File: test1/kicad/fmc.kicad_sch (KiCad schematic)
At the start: 0 parts

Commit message: test1: fill in Power, Bias, Bobcat, Connectors, FMC sheets
Completes the test1 Bobcat carrier hierarchical schematic. All 7 sheets
(root + 6 children) parse cleanly with kicad-cli and render to SVG/PDF.

Contents per child:
  - power.kicad_sch       — TPS7A8401A LDO (3P3V → 0.8V via ANY-OUT
                            strap, OUT side fans to +VDDD/+VDDA1/+VDDA2
                            via 1×2 jumpers) + TPS22916 load switch
                            (VADJ → +VDDIO) with EN pulldowns + decoupling.
  - bobcat.kicad_sch      — Bobcat 40-QFN DUT with VDDD/VDDIO decoupling,
                            VDDA1/VDDA2 series 0Ω + decoupling, hier-label
                            exits on all four edges for SAMPLE_OUT*,
                            SPI, GPIO, CLK_OUT*, BIAS0/1, etc.
  - eeprom.kicad_sch      — 24AA08 I²C EEPROM (address 000, WP→GND,
                            0.1 µF decoupling, 2.2 kΩ I²C pull-ups).
  - bias.kicad_sch        — MCP4728 quad DAC + OPA2388 dual op-amp
                            (units 1 & 2) + PMZ1200UPEYL high-side PMOS
                            × 2 channels + 5.11 kΩ 0.1% sense resistors +
                            DNP 2N7002 isolation NMOS placeholders.
  - connectors.kicad_sch  — 4× SMA for CLK_OUT0–3, 3× SMA for
                            OSC_EN/WEIGHT_EN/SAMPLE_TRIG, 1×4 GPIO
                            header, 3× Keystone-5011 GND test clips.
  - fmc.kicad_sch         — VITA 57.1 LPC connector (4 units × 40 pins),
                            wired for 3P3V/VADJ/SCL/SDA/PRSNT/GA0/GA1/
                            PG_C2M/LDO_EN/LSW_EN; LA-bank pins NC'd for
                            later pinning; all other C/D/G/H pins to GND.

Generator improvements driven by this round:
  - Multi-unit symbol support (parse_pins now returns the per-pin unit
    number; place() takes a unit= parameter and emits matching (unit N)
    in the instance + path).
  - Escape backslash/quote in property values so refs/values with
    embedded " (e.g. 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
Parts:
- added J1: FMC LPC (C), Connector:FMC_LPC_ASP-134606-01, symbol Lib:ASP-134606-01
- added J2: FMC LPC (D), Connector:FMC_LPC_ASP-134606-01, symbol Lib:ASP-134606-01
- added J3: FMC LPC (G), Connector:FMC_LPC_ASP-134606-01, symbol Lib:ASP-134606-01
- added J4: FMC LPC (H), Connector:FMC_LPC_ASP-134606-01, symbol Lib:ASP-134606-01
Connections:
- new net +3V3: J1.C36, J1.C38, J1.C40, J2.D39
- new net GND: J1.C10, J1.C13, J1.C16, J1.C19, J1.C2, J1.C22, J1.C25, J1.C28, J1.C3, J1.C34, J1.C35, J1.C37, J1.C39, J1.C6, J1.C7, J2.D1, J2.D12, J2.D13, J2.D16, J2.D17, J2.D20, J2.D21, J2.D24, J2.D25, J2.D28, J2.D29, J2.D32, J2.D33, J2.D34, J2.D36, J2.D38, J2.D4, J2.D40, J2.D5, J2.D8, J2.D9, J3.G1, J3.G12, J3.G15, J3.G18, J3.G2, J3.G21, J3.G24, J3.G27, J3.G3, J3.G30, J3.G33, J3.G36, J3.G39, J3.G6, J3.G9, J4.H11, J4.H14, J4.H17, J4.H2, J4.H20, J4.H23, J4.H26, J4.H29, J4.H32, J4.H35, J4.H38, J4.H4, J4.H40, J4.H5, J4.H8
- new net LDO_PG: J1.C1
- new net SCL: J2.D30
- new net SDA: J2.D31
- new net VADJ: J3.G40, J4.H39
- no-connect marks 0 -> 85
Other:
- title: test1 — FMC Connector -> test1 — FMC LPC Connector (Power + I²C only)

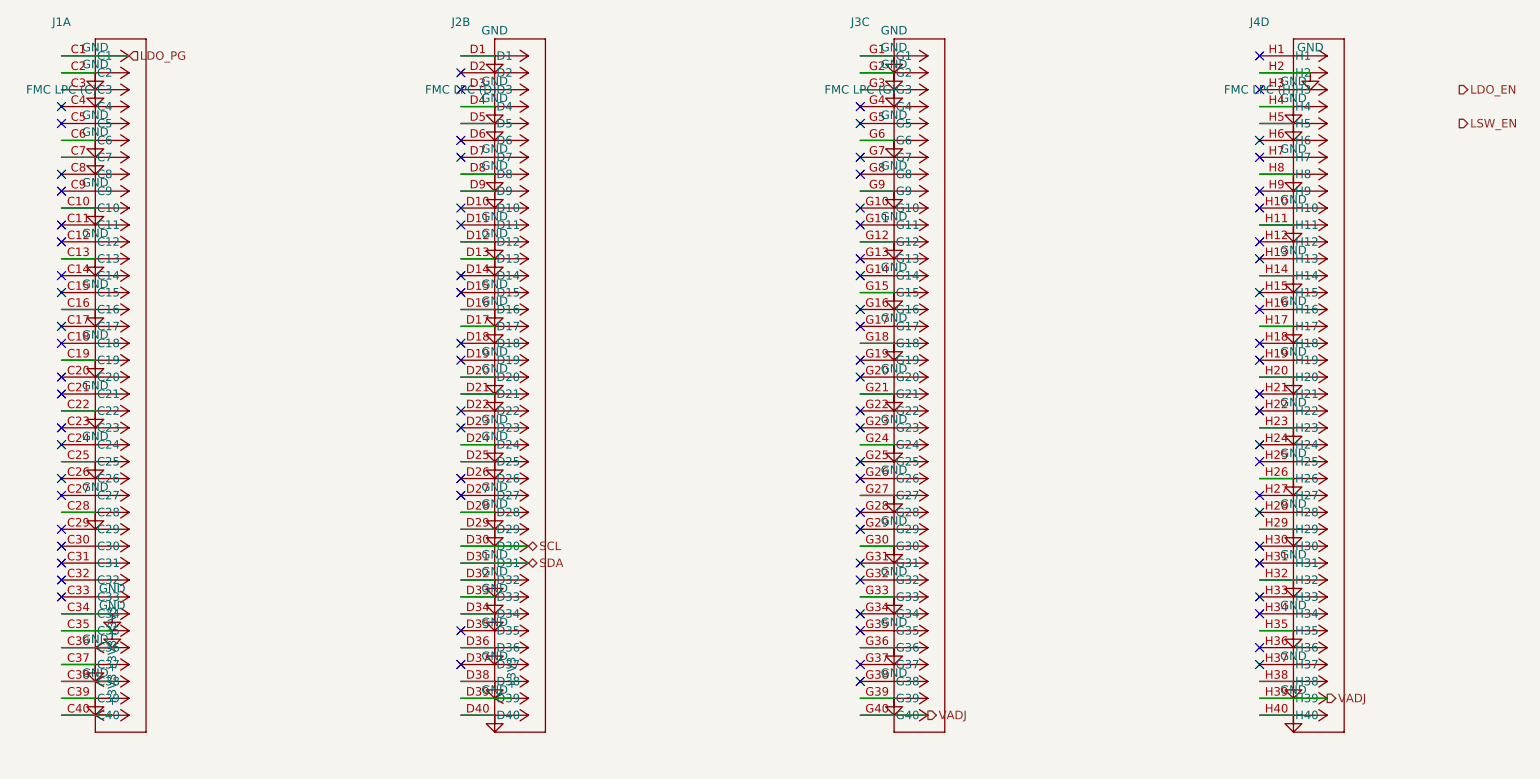
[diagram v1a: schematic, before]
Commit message: Apply layout best-practices from reference schematic
Skill updates (from the LTC3114 reference sample):
  - New rule 5: no net passes through a component body (visual ambiguity).
  - New rule 6: every placed component is in-path or removed — DNP parts
    stay wired in series and just carry (dnp yes) + "DNP" value tag; never
    leave a part with no_connect on all its pins as a "for later"
    placeholder.
  - New rule 7: GND symbols cluster — one (power:GND) per local pin group,
    not one per pin. Connector banks bus their GNDs onto a single rail
    with one terminating triangle.
  - New rule 8: canonical decoupling-cap cluster (bulk+HF share one rail
    above and one GND below; stay off the path of unrelated nets).

test1 design fixes (each addresses a specific point raised on review):

  1. Bias: Q3, Q4 (2N7002 NMOS isolators) now wired in series between
     each PMOS drain and the BIASx output — gates exit as BIAS_ISO0 /
     BIAS_ISO1 hier labels for MCU control. Marked DNP via "2N7002 DNP"
     value. No more orphaned no_connects.

  2. Bobcat: VDDA2 decoupling cap C4 moved onto its own branch BELOW the
     R6 series-0Ω lane, off the pin-26/27 tie wire path.

  3. FMC: ~150 individual per-pin GND symbols collapsed into one
     consolidated GND rail per unit (J1/J2/J3/J4), each terminating in a
     single GND triangle at the rail's bottom.

  4. Power: TPS22916 (U2) decoupling caps C6 and C7 moved ALONGSIDE the
     chip body (left and right) at the same y as VIN/VOUT — wires no
     longer pass under the chip footprint. Cap pin 1 (top) → chip pin
     via horizontal stub; cap pin 2 (bot) → GND rail below.

Co-Authored-By: Claude Opus 4.7 (1M context) <noreply@anthropic.com>
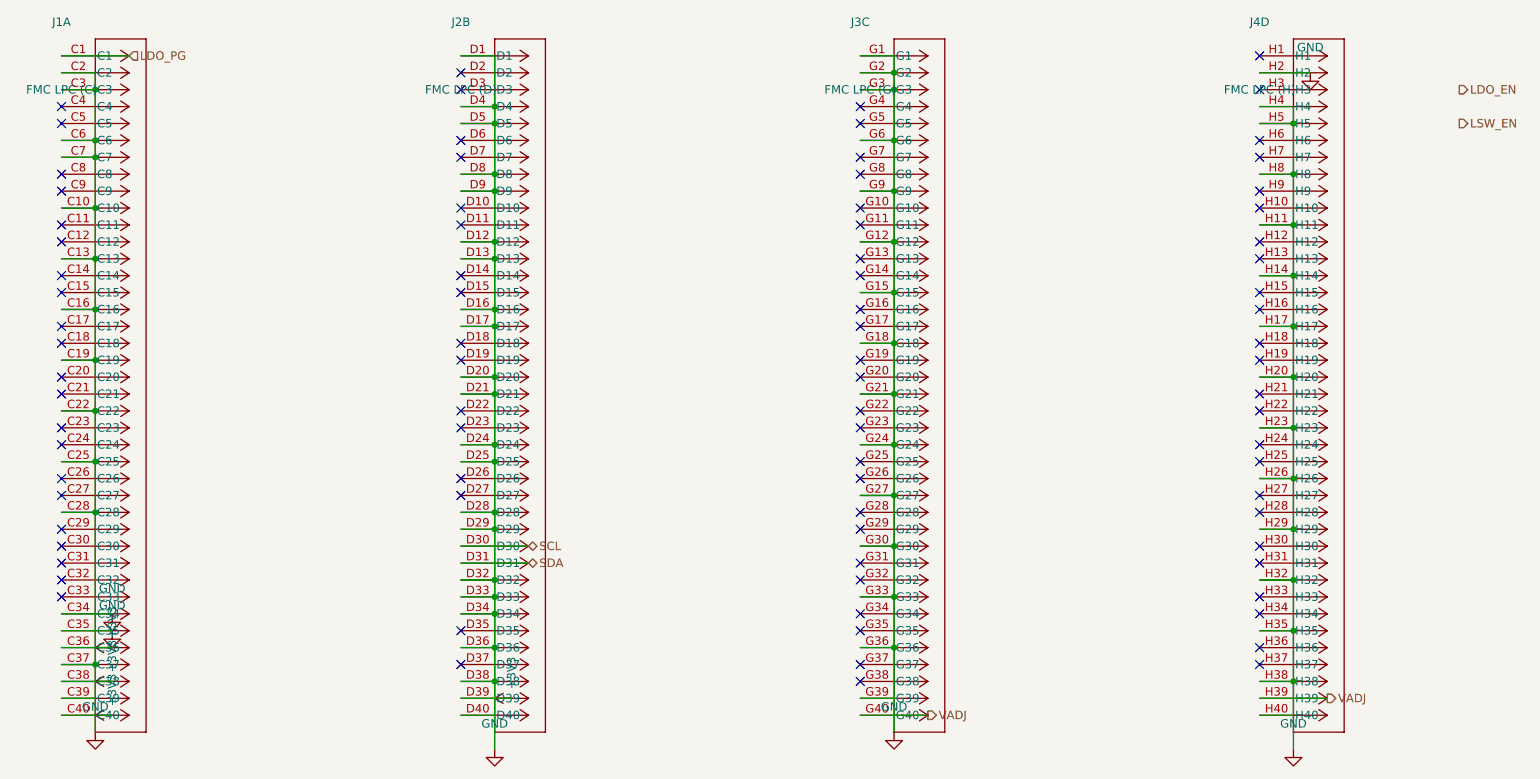
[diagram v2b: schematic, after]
